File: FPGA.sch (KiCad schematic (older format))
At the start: 42 parts

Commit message: Reorganize FPGA schematic
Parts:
- added C?: 100n, symbol Device:C
- added J?: Conn_02x07_Odd_Even, symbol Connector_Generic:Conn_02x07_Odd_Even
- added R? (x2): 10k, symbol Device:R
- added R? (x4): 4.7k, symbol Device:R
- added R?: 330, symbol Device:R
- added R?: 2.4k, symbol Device:R
- added U? (x3): XC7A100T-FTG256, symbol FPGA_Xilinx_Artix7:XC7A100T-FTG256
- added U?: AS6C1616, Package_SO:TSOP-I-48_18.4x12mm_P0.5mm, symbol Memory_RAM:AS6C1616
- added U?: S25FL1, symbol flash_memory:S25FL1
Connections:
- net +3V3: now also C?.1, J?.2 (Pin_2), R?.1, R?.1, R?.1, R?.1, R?.1, R?.1, R?.1, R?.2, U?.37 (VCC), U?.8 (VCC), U?.A6 (VCCO_35), U?.B3 (VCCO_35), U?.D7 (VCCO_35), U?.E4 (VCCO_35), U?.E7 (CFGBVS_0), U?.F1 (VCCO_35), U?.J2 (VCCO_35), U?.L16 (VCCO_14), U?.L6 (VCCO_0), U?.M13 (VCCO_14), U?.M9 (M0_0), U?.N10 (VCCO_14), U?.P7 (VCCO_14), U?.R14 (VCCO_14), U?.T11 (VCCO_14)
- net GND: now also C?.2, J?.1 (Pin_1), J?.11 (Pin_11), J?.13 (Pin_13), J?.3 (Pin_3), J?.5 (Pin_5), J?.7 (Pin_7), J?.9 (Pin_9), U?.27 (VSS), U?.4 (GND), U?.46 (VSS), U?.A16 (VCCO_15), U?.B13 (VCCO_15), U?.C10 (VCCO_15), U?.E14 (VCCO_15), U?.H15 (VCCO_15), U?.H7 (VREFN_0), U?.H8 (VP_0), U?.J12 (VCCO_15), U?.J7 (VN_0), U?.J8 (VREFP_0), U?.M10 (M1_0), U?.M11 (M2_0), U?.M3 (VCCO_34), U?.R4 (VCCO_34), U?.T1 (VCCO_34)
- net at U?.5 (OUT): now also U?.N14 (IO_L12P_T1_MRCC_14)
- new net: U?.6 (CLK), U?.E8 (CCLK_0)
- new net: R?.2, U?.K10 (INIT_B_0)
- new net: J?.6 (Pin_6), R?.2, U?.L7 (TCK_0)
- new net: J?.4 (Pin_4), R?.2, U?.M7 (TMS_0)
- new net: J?.10 (Pin_10), U?.N7 (TDI_0)
- new net: J?.8 (Pin_8), U?.N8 (TDO_0)
- new net: U?.5 (SI/IO0), U?.J13 (IO_L1P_T0_D00_MOSI_14)
- new net: U?.2 (SO/IO1), U?.J14 (IO_L1N_T0_D01_DIN_14)
- new net: R?.2, U?.3 (WP#/IO2), U?.K15 (IO_L2P_T0_D02_14)
- new net: R?.2, U?.7 (HOLD#/RESET#/IO3), U?.K16 (IO_L2N_T0_D03_14)
- new net: R?.2, U?.1 (CS#), U?.L12 (IO_L6P_T0_FCS_B_14)
- new net SRAM_a0: U?.25 (A0), U?.A2 (IO_L8N_T1_AD14N_35)
- new net SRAM_a1: U?.24 (A1), U?.C1 (IO_L9P_T1_DQS_AD7P_35)
- new net SRAM_a10: U?.6 (A10), U?.E5 (IO_L13N_T2_MRCC_35)
- new net SRAM_a11: U?.5 (A11), U?.F4 (IO_L14P_T2_SRCC_35)
- new net SRAM_a12: U?.4 (A12), U?.F3 (IO_L14N_T2_SRCC_35)
- new net SRAM_a13: U?.3 (A13), U?.F2 (IO_L15P_T2_DQS_35)
- new net SRAM_a14: U?.2 (A14), U?.E1 (IO_L15N_T2_DQS_35)
- new net SRAM_a15: U?.1 (A15), U?.G5 (IO_L16P_T2_35)
- new net SRAM_a16: U?.48 (A16), U?.G4 (IO_L16N_T2_35)
- new net SRAM_a17: U?.17 (A17), U?.G2 (IO_L17P_T2_35)
- new net SRAM_a18: U?.16 (A18), U?.G1 (IO_L17N_T2_35)
- new net SRAM_a19: U?.9 (A19), U?.H5 (IO_L18P_T2_35)
- new net SRAM_a2: U?.23 (A2), U?.B1 (IO_L9N_T1_DQS_AD7N_35)
- new net SRAM_a3: U?.22 (A3), U?.E2 (IO_L10P_T1_AD15P_35)
- new net SRAM_a4: U?.21 (A4), U?.D1 (IO_L10N_T1_AD15N_35)
- new net SRAM_a5: U?.20 (A5), U?.E3 (IO_L11P_T1_SRCC_35)
- new net SRAM_a6: U?.19 (A6), U?.D3 (IO_L11N_T1_SRCC_35)
- new net SRAM_a7: U?.18 (A7), U?.D4 (IO_L12P_T1_MRCC_35)
- new net SRAM_a8: U?.8 (A8), U?.C4 (IO_L12N_T1_MRCC_35)
- new net SRAM_a9: U?.7 (A9), U?.F5 (IO_L13P_T2_MRCC_35)
- new net SRAM_ce#: U?.26 (CE#), U?.J4 (IO_L19N_T3_VREF_35)
- new net SRAM_ce2: U?.12 (CE2), U?.H2 (IO_L20P_T3_35)
- new net SRAM_dio0: U?.29 (DQ0), U?.E6 (IO_0_35)
- new net SRAM_dio1: U?.31 (DQ1), U?.B7 (IO_L1P_T0_AD4P_35)
- new net SRAM_dio10: U?.34 (DQ10), U?.C6 (IO_L5N_T0_AD13N_35)
- new net SRAM_dio11: U?.36 (DQ11), U?.D6 (IO_L6P_T0_35)
- new net SRAM_dio12: U?.39 (DQ12), U?.D5 (IO_L6N_T0_VREF_35)
- new net SRAM_dio13: U?.41 (DQ13), U?.C3 (IO_L7P_T1_AD6P_35)
- new net SRAM_dio14: U?.43 (DQ14), U?.C2 (IO_L7N_T1_AD6N_35)
- new net SRAM_dio15: U?.45 (DQ15), U?.B2 (IO_L8P_T1_AD14P_35)
- new net SRAM_dio2: U?.33 (DQ2), U?.A7 (IO_L1N_T0_AD4N_35)
- new net SRAM_dio3: U?.35 (DQ3), U?.B6 (IO_L2P_T0_AD12P_35)
- new net SRAM_dio4: U?.38 (DQ4), U?.B5 (IO_L2N_T0_AD12N_35)
- new net SRAM_dio5: U?.40 (DQ5), U?.A5 (IO_L3P_T0_DQS_AD5P_35)
- new net SRAM_dio6: U?.42 (DQ6), U?.A4 (IO_L3N_T0_DQS_AD5N_35)
- new net SRAM_dio7: U?.44 (DQ7), U?.B4 (IO_L4P_T0_35)
- new net SRAM_dio8: U?.30 (DQ8), U?.A3 (IO_L4N_T0_35)
- new net SRAM_dio9: U?.32 (DQ9), U?.C7 (IO_L5P_T0_AD13P_35)
- new net SRAM_lb#: U?.15 (LB#), U?.J3 (IO_L21P_T3_DQS_35)
- new net SRAM_oe#: U?.28 (OE#), U?.H4 (IO_L18N_T2_35)
- new net SRAM_ub#: U?.14 (UB#), U?.H1 (IO_L20N_T3_35)
- new net SRAM_we#: U?.11 (WE#), U?.J5 (IO_L19P_T3_35)
- new net done: R?.2, U?.H10 (DONE_0)
- new net program_b: R?.1, U?.L9 (PROGRAM_B_0)
- no-connect marks 1 -> 83
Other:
- moved on the sheet: C?, U?

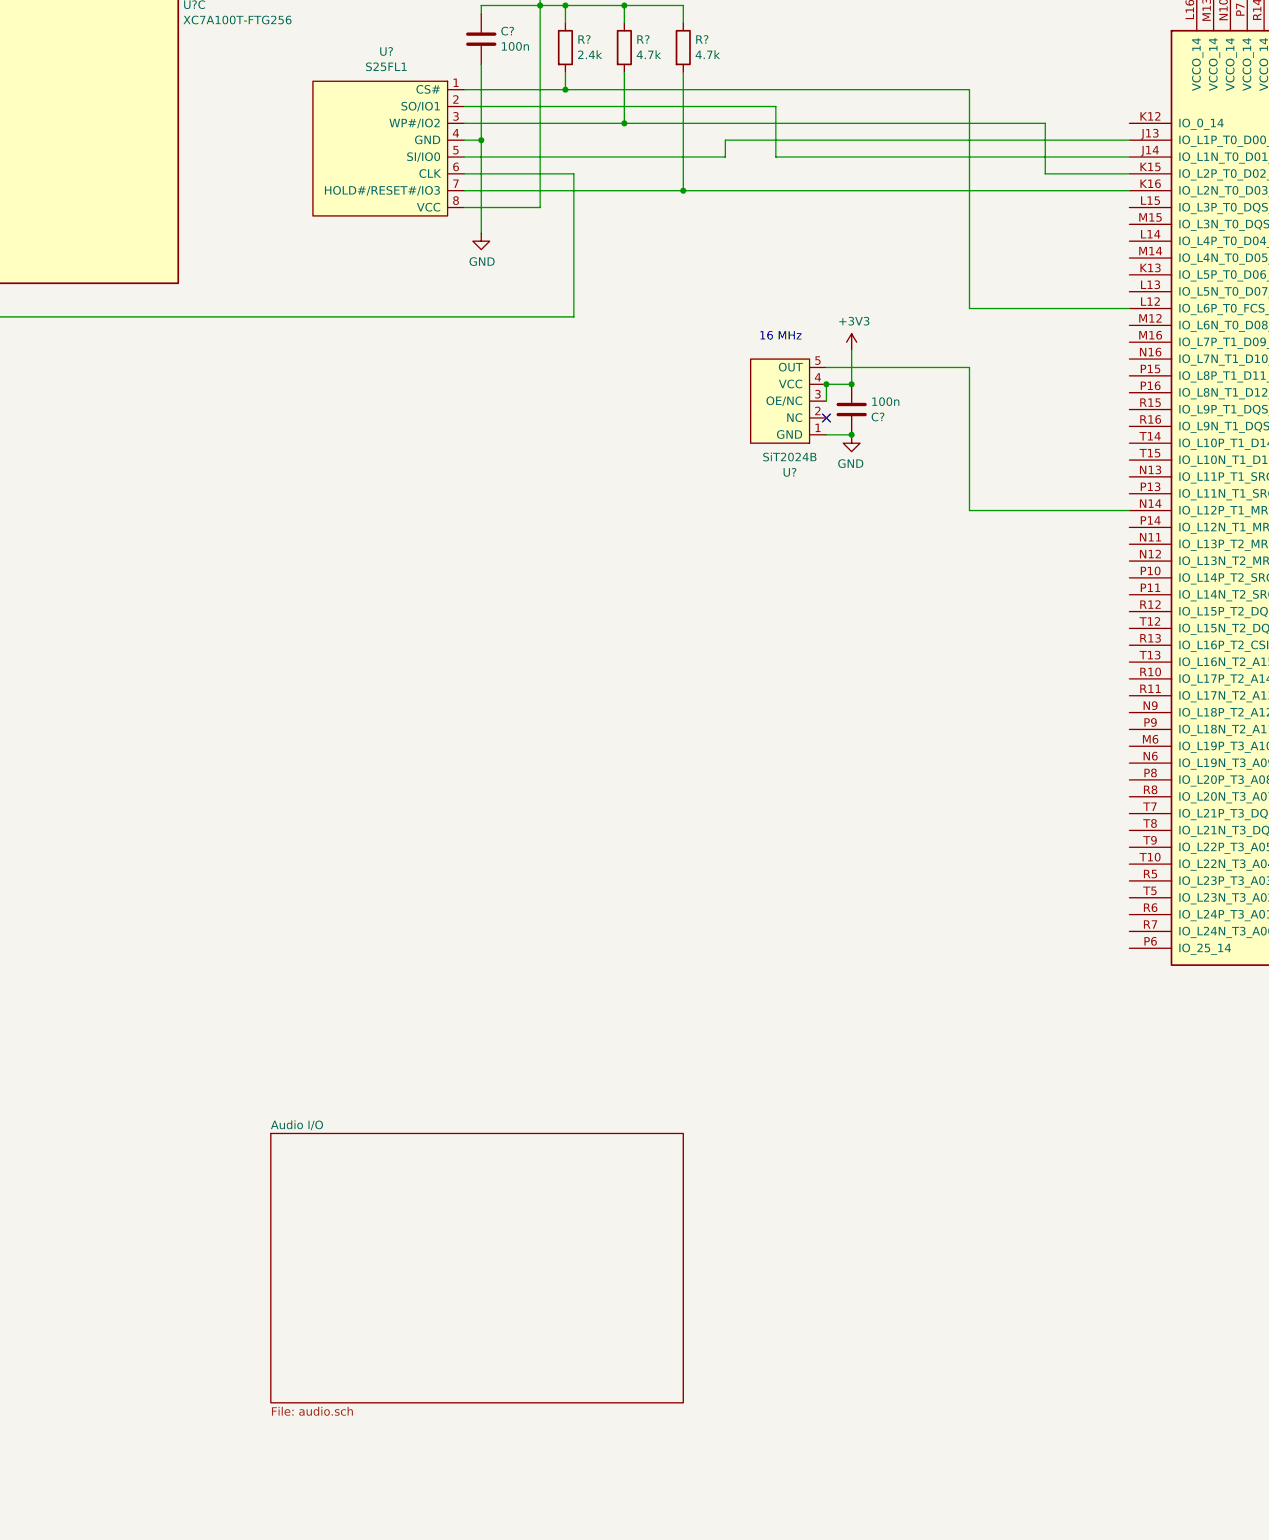
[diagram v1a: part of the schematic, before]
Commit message: Prepare FPGA I/O pins
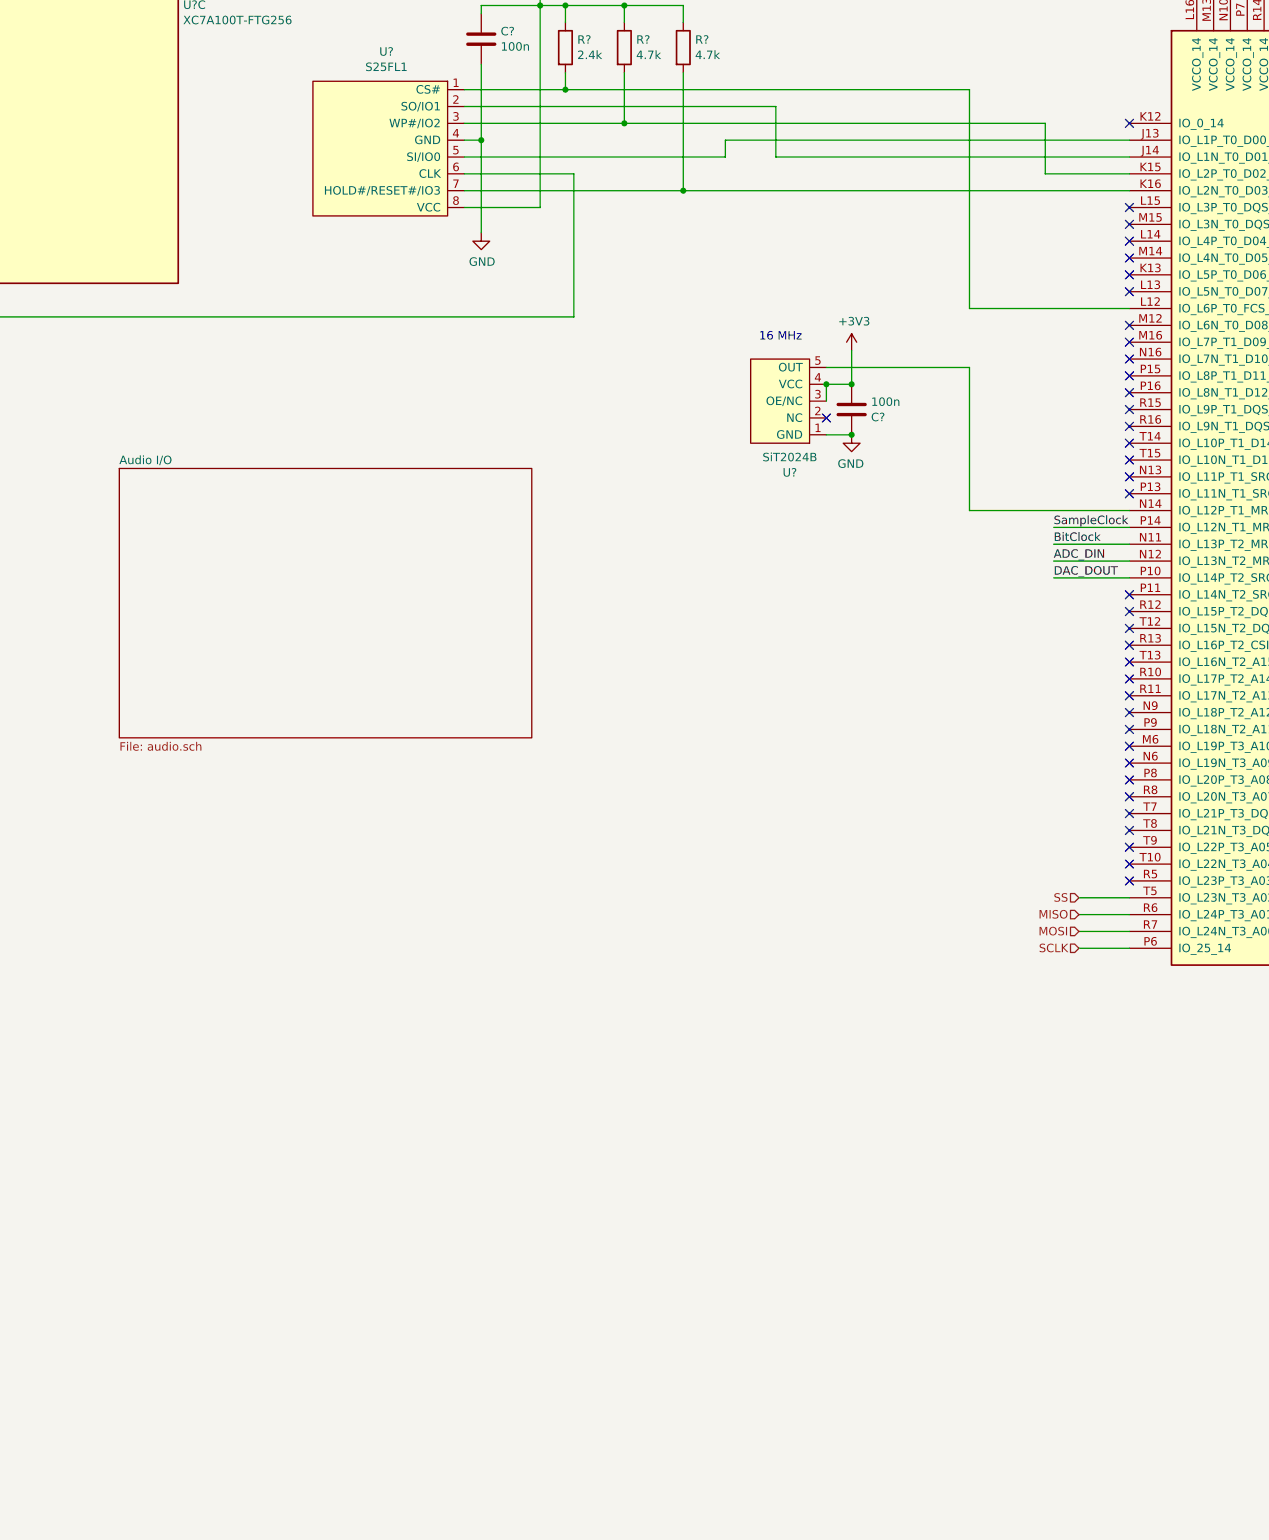
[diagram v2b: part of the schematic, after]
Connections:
- net BitClock: now reaches U?.N11 (IO_L13P_T2_MRCC_14)
- net ADC_DIN: now reaches U?.N12 (IO_L13N_T2_MRCC_14)
- net DAC_DOUT: now reaches U?.P10 (IO_L14P_T2_SRCC_14)
- net SampleClock: now reaches U?.P14 (IO_L12N_T1_MRCC_14)
- net SCLK: now reaches U?.P6 (IO_25_14)
- net MISO: now reaches U?.R6 (IO_L24P_T3_A01_D17_14)
- net MOSI: now reaches U?.R7 (IO_L24N_T3_A00_D16_14)
- net SS: now reaches U?.T5 (IO_L23N_T3_A02_D18_14)
- no-connect marks 83 -> 119
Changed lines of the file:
@@
 $EndDescr
 $Sheet
-S 1850 5950 2450 1600
+S 950  2000 2450 1600
 U 5D7E4A66
 F0 "Audio I/O" 50
@@
 Connection ~ 7600 13000
 $Comp
-L power:GND #PWR?
+L power:GND #PWR0124
 U 1 1 5E505D4A
 P 13450 1300
-AR Path="/5D7D43D9/5E505D4A" Ref="#PWR?"  Part="1"
+AR Path="/5D7D43D9/5E505D4A" Ref="#PWR0124"  Part="1"
 AR Path="/5D7D43D9/5DD5155F/5E505D4A" Ref="#PWR?"  Part="1"
 AR Path="/5D7D43D9/5E0EF1ED/5E505D4A" Ref="#PWR?"  Part="1"
-F 0 "#PWR?" H 13450 1050 50  0001 C CNN
+F 0 "#PWR0124" H 13450 1050 50  0001 C CNN
 F 1 "GND" H 13455 1127 50  0000 C CNN
 F 2 "" H 13450 1300 50  0001 C CNN
@@
 P 15550 1300
 AR Path="/5D7D43D9/5E0EF1ED/5E505D64" Ref="#PWR?"  Part="1"
-AR Path="/5D7D43D9/5E505D64" Ref="#PWR?"  Part="1"
-F 0 "#PWR?" H 15550 1150 50  0001 C CNN
+AR Path="/5D7D43D9/5E505D64" Ref="#PWR0125"  Part="1"
+F 0 "#PWR0125" H 15550 1150 50  0001 C CNN
 F 1 "+3V3" H 15565 1473 50  0000 C CNN
 F 2 "" H 15550 1300 50  0001 C CNN
@@
 P 19450 4450
 AR Path="/5D7D43D9/5E0EF1ED/5E505DDB" Ref="#PWR?"  Part="1"
-AR Path="/5D7D43D9/5E505DDB" Ref="#PWR?"  Part="1"
-F 0 "#PWR?" H 19450 4200 50  0001 C CNN
+AR Path="/5D7D43D9/5E505DDB" Ref="#PWR0126"  Part="1"
+F 0 "#PWR0126" H 19450 4200 50  0001 C CNN
 F 1 "GND" H 19455 4277 50  0000 C CNN
 F 2 "" H 19450 4450 50  0001 C CNN
@@
 P 19850 1400
 AR Path="/5D7D43D9/5E0EF1ED/5E505DED" Ref="#PWR?"  Part="1"
-AR Path="/5D7D43D9/5E505DED" Ref="#PWR?"  Part="1"
-F 0 "#PWR?" H 19850 1250 50  0001 C CNN
+AR Path="/5D7D43D9/5E505DED" Ref="#PWR0127"  Part="1"
+F 0 "#PWR0127" H 19850 1250 50  0001 C CNN
 F 1 "+3V3" H 19865 1573 50  0000 C CNN
 F 2 "" H 19850 1400 50  0001 C CNN
@@
 $EndComp
 $Comp
-L power:+3V3 #PWR?
+L power:+3V3 #PWR0128
 U 1 1 5E538FEB
 P -1050 -2450
-AR Path="/5D7D43D9/5E538FEB" Ref="#PWR?"  Part="1"
+AR Path="/5D7D43D9/5E538FEB" Ref="#PWR0128"  Part="1"
 AR Path="/5D7D43D9/5DD5155F/5E538FEB" Ref="#PWR?"  Part="1"
-F 0 "#PWR?" H -1050 -2600 50  0001 C CNN
+F 0 "#PWR0128" H -1050 -2600 50  0001 C CNN
 F 1 "+3V3" H -1035 -2277 50  0000 C CNN
 F 2 "" H -1050 -2450 50  0001 C CNN
@@
 P -4750 -250
 AR Path="/5D7D43D9/5DD5155F/5E538FF8" Ref="#PWR?"  Part="1"
-AR Path="/5D7D43D9/5E538FF8" Ref="#PWR?"  Part="1"
-F 0 "#PWR?" H -4750 -500 50  0001 C CNN
+AR Path="/5D7D43D9/5E538FF8" Ref="#PWR0129"  Part="1"
+F 0 "#PWR0129" H -4750 -500 50  0001 C CNN
 F 1 "GND" H -4745 -423 50  0000 C CNN
 F 2 "" H -4750 -250 50  0001 C CNN
@@
 P -3300 -2000
 AR Path="/5D7D43D9/5DD5155F/5E53900B" Ref="#PWR?"  Part="1"
-AR Path="/5D7D43D9/5E53900B" Ref="#PWR?"  Part="1"
-F 0 "#PWR?" H -3300 -2150 50  0001 C CNN
+AR Path="/5D7D43D9/5E53900B" Ref="#PWR0130"  Part="1"
+F 0 "#PWR0130" H -3300 -2150 50  0001 C CNN
 F 1 "+3V3" H -3285 -1827 50  0000 C CNN
 F 2 "" H -3300 -2000 50  0001 C CNN
@@
 P -1650 500
 AR Path="/5D7D43D9/5DD5155F/5E539066" Ref="#PWR?"  Part="1"
-AR Path="/5D7D43D9/5E539066" Ref="#PWR?"  Part="1"
-F 0 "#PWR?" H -1650 250 50  0001 C CNN
+AR Path="/5D7D43D9/5E539066" Ref="#PWR0131"  Part="1"
+F 0 "#PWR0131" H -1650 250 50  0001 C CNN
 F 1 "GND" H -1645 327 50  0000 C CNN
 F 2 "" H -1650 500 50  0001 C CNN
@@
 $EndComp
 $Comp
-L power:+3V3 #PWR?
+L power:+3V3 #PWR0132
 U 1 1 5E539084
 P 7350 -950
-AR Path="/5D7D43D9/5E539084" Ref="#PWR?"  Part="1"
+AR Path="/5D7D43D9/5E539084" Ref="#PWR0132"  Part="1"
 AR Path="/5D7D43D9/5DD5155F/5E539084" Ref="#PWR?"  Part="1"
-F 0 "#PWR?" H 7350 -1100 50  0001 C CNN
+F 0 "#PWR0132" H 7350 -1100 50  0001 C CNN
 F 1 "+3V3" H 7365 -777 50  0000 C CNN
 F 2 "" H 7350 -950 50  0001 C CNN
@@
 	10450 -850 10550 -850
 $Comp
-L power:GND #PWR?
+L power:GND #PWR0133
 U 1 1 5E53909E
 P 10750 -850
-AR Path="/5D7D43D9/5E53909E" Ref="#PWR?"  Part="1"
+AR Path="/5D7D43D9/5E53909E" Ref="#PWR0133"  Part="1"
 AR Path="/5D7D43D9/5DD5155F/5E53909E" Ref="#PWR?"  Part="1"
-F 0 "#PWR?" H 10750 -1100 50  0001 C CNN
+F 0 "#PWR0133" H 10750 -1100 50  0001 C CNN
 F 1 "GND" H 10755 -1023 50  0000 C CNN
 F 2 "" H 10750 -850 50  0001 C CNN
@@
 P 3450 -850
 AR Path="/5D7D43D9/5DD5155F/5E5390EE" Ref="#PWR?"  Part="1"
-AR Path="/5D7D43D9/5E5390EE" Ref="#PWR?"  Part="1"
-F 0 "#PWR?" H 3450 -1000 50  0001 C CNN
+AR Path="/5D7D43D9/5E5390EE" Ref="#PWR0134"  Part="1"
+F 0 "#PWR0134" H 3450 -1000 50  0001 C CNN
 F 1 "+3V3" H 3465 -677 50  0000 C CNN
 F 2 "" H 3450 -850 50  0001 C CNN
@@
 P 3100 600
 AR Path="/5D7D43D9/5DD5155F/5E53911A" Ref="#PWR?"  Part="1"
-AR Path="/5D7D43D9/5E53911A" Ref="#PWR?"  Part="1"
-F 0 "#PWR?" H 3100 350 50  0001 C CNN
+AR Path="/5D7D43D9/5E53911A" Ref="#PWR0135"  Part="1"
+F 0 "#PWR0135" H 3100 350 50  0001 C CNN
 F 1 "GND" H 3105 427 50  0000 C CNN
 F 2 "" H 3100 600 50  0001 C CNN
@@
 Wire Wire Line
 	6000 2250 6950 2250
+NoConn ~ 6950 -50
+NoConn ~ 6950 450
+NoConn ~ 6950 550
+NoConn ~ 6950 650
+NoConn ~ 6950 750
+NoConn ~ 6950 850
+NoConn ~ 6950 950
+Text Label 6500 2350 0    50   ~ 0
+SampleClock
+Wire Wire Line
+	6950 2350 6500 2350
+Text Label 6500 2450 0    50   ~ 0
+BitClock
+Wire Wire Line
+	6500 2450 6950 2450
+Text Label 6500 2550 0    50   ~ 0
+ADC_DIN
+Wire Wire Line
+	6500 2550 6950 2550
+Text Label 6500 2650 0    50   ~ 0
+DAC_DOUT
+Wire Wire Line
+	6500 2650 6950 2650
+Text HLabel 6650 4850 0    50   Input ~ 0
+SCLK
+Text HLabel 6650 4750 0    50   Input ~ 0
+MOSI
+Text HLabel 6650 4650 0    50   Input ~ 0
+MISO
+Text HLabel 6650 4550 0    50   Input ~ 0
+SS
+Wire Wire Line
+	6650 4550 6950 4550
+Wire Wire Line
+	6650 4650 6950 4650
+Wire Wire Line
+	6650 4750 6950 4750
+Wire Wire Line
+	6650 4850 6950 4850
+NoConn ~ 6950 1150
+NoConn ~ 6950 1250
+NoConn ~ 6950 1350
+NoConn ~ 6950 1450
+NoConn ~ 6950 1550
+NoConn ~ 6950 1650
+NoConn ~ 6950 1750
+NoConn ~ 6950 1850
+NoConn ~ 6950 1950
+NoConn ~ 6950 2050
+NoConn ~ 6950 2150
+NoConn ~ 6950 2750
+NoConn ~ 6950 2850
+NoConn ~ 6950 2950
+NoConn ~ 6950 3050
+NoConn ~ 6950 3150
+NoConn ~ 6950 3250
+NoConn ~ 6950 3350
+NoConn ~ 6950 3450
+NoConn ~ 6950 3550
+NoConn ~ 6950 3650
+NoConn ~ 6950 3750
+NoConn ~ 6950 3850
+NoConn ~ 6950 3950
+NoConn ~ 6950 4050
+NoConn ~ 6950 4150
+NoConn ~ 6950 4250
+NoConn ~ 6950 4350
+NoConn ~ 6950 4450
 $EndSCHEMATC

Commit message: FPGA cleanup
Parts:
- added J2: 26642801RP2, CON28_2X14_HDR_2664, symbol pin_header:26642801RP2
- U3: renamed from U?; footprint (none) -> Package_BGA:Xilinx_FTG256
- U4: renamed from U?; footprint (none) -> Package_SO:SOIC-8_5.275x5.275mm_P1.27mm
- U5: renamed from U?; footprint (none) -> Package_TO_SOT_SMD:SOT-23-5
- gave numbers to parts that had none: 52
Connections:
- net ADC_DIN: now also U3.M14 (IO_L4N_T0_D05_14); no longer U3.N12 (IO_L13N_T2_MRCC_14)
- net BitClock: now also U3.L14 (IO_L4P_T0_D04_14); no longer U3.N11 (IO_L13P_T2_MRCC_14)
- net DAC_DOUT: now also U3.K13 (IO_L5P_T0_D06_14); no longer U3.P10 (IO_L14P_T2_SRCC_14)
- net MISO: now also U3.R15 (IO_L9P_T1_DQS_14); no longer U3.R6 (IO_L24P_T3_A01_D17_14)
- net MOSI: now also U3.R16 (IO_L9N_T1_DQS_D13_14); no longer U3.R7 (IO_L24N_T3_A00_D16_14)
- net SCLK: now also U3.T14 (IO_L10P_T1_D14_14); no longer U3.P6 (IO_25_14)
- net SS: now also U3.P16 (IO_L8N_T1_D12_14); no longer U3.T5 (IO_L23N_T3_A02_D18_14)
- net SampleClock: now also U3.M15 (IO_L3N_T0_DQS_EMCCLK_14); no longer U3.P14 (IO_L12N_T1_MRCC_14)
- net GPIO_3: now reaches U3.M12 (IO_L6N_T0_D08_VREF_14)
- net GPIO_2: now reaches U3.M16 (IO_L7P_T1_D09_14)
- net FPGA_pinout_14: now reaches U3.M6 (IO_L19P_T3_A10_D26_14)
- net FPGA_pinout_14: now also J2.14
- net GPIO_1: now reaches U3.N16 (IO_L7N_T1_D10_14)
- net FPGA_pinout_15: now reaches U3.N6 (IO_L19N_T3_A09_D25_VREF_14)
- net FPGA_pinout_15: now also J2.15
- net FPGA_pinout_12: now reaches U3.N9 (IO_L18P_T2_A12_D28_14)
- net FPGA_pinout_12: now also J2.12
- net FPGA_pinout_5: now reaches U3.P11 (IO_L14N_T2_SRCC_14)
- net FPGA_pinout_5: now also J2.5
- net GPIO_0: now reaches U3.P15 (IO_L8P_T1_D11_14)
- net FPGA_pinout_16: now reaches U3.P8 (IO_L20P_T3_A08_D24_14)
- net FPGA_pinout_16: now also J2.16
- net FPGA_pinout_13: now reaches U3.P9 (IO_L18N_T2_A11_D27_14)
- net FPGA_pinout_13: now also J2.13
- net FPGA_pinout_10: now reaches U3.R10 (IO_L17P_T2_A14_D30_14)
- net FPGA_pinout_10: now also J2.10
- net FPGA_pinout_11: now reaches U3.R11 (IO_L17N_T2_A13_D29_14)
- net FPGA_pinout_11: now also J2.11
- net FPGA_pinout_6: now reaches U3.R12 (IO_L15P_T2_DQS_RDWR_B_14)
- net FPGA_pinout_6: now also J2.6
- net FPGA_pinout_8: now reaches U3.R13 (IO_L16P_T2_CSI_B_14)
- net FPGA_pinout_8: now also J2.8
- net FPGA_pinout_22: now reaches U3.R5 (IO_L23P_T3_A03_D19_14)
- net FPGA_pinout_22: now also J2.22
- net FPGA_pinout_17: now reaches U3.R8 (IO_L20N_T3_A07_D23_14)
- net FPGA_pinout_17: now also J2.17
- net FPGA_pinout_21: now reaches U3.T10 (IO_L22N_T3_A04_D20_14)
- net FPGA_pinout_21: now also J2.21
- net FPGA_pinout_7: now reaches U3.T12 (IO_L15N_T2_DQS_DOUT_CSO_B_14)
- net FPGA_pinout_7: now also J2.7
- net FPGA_pinout_9: now reaches U3.T13 (IO_L16N_T2_A15_D31_14)
- net FPGA_pinout_9: now also J2.9
- net FPGA_pinout_18: now reaches U3.T7 (IO_L21P_T3_DQS_14)
- net FPGA_pinout_18: now also J2.18
- net FPGA_pinout_19: now reaches U3.T8 (IO_L21N_T3_DQS_A06_D22_14)
- net FPGA_pinout_19: now also J2.19
- net FPGA_pinout_20: now reaches U3.T9 (IO_L22P_T3_A05_D21_14)
- net FPGA_pinout_20: now also J2.20
- new net FPGA_pinout_1: J2.1, U3.P14 (IO_L12N_T1_MRCC_14)
- new net FPGA_pinout_2: J2.2, U3.N11 (IO_L13P_T2_MRCC_14)
- new net FPGA_pinout_23: J2.23, U3.T5 (IO_L23N_T3_A02_D18_14)
- new net FPGA_pinout_24: J2.24, U3.R6 (IO_L24P_T3_A01_D17_14)
- new net FPGA_pinout_25: J2.25, U3.R7 (IO_L24N_T3_A00_D16_14)
- new net FPGA_pinout_26: J2.26, U3.P6 (IO_25_14)
- new net FPGA_pinout_3: J2.3, U3.N12 (IO_L13N_T2_MRCC_14)
- new net FPGA_pinout_4: J2.4, U3.P10 (IO_L14P_T2_SRCC_14)
- no-connect marks 119 -> 91
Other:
- note added: "Vccaux"
- note added: "Vccbram"
- note added: "Vcco"
- moved on the sheet: C20, C25, J1, R10, R11, R12, R13, R14, R15, R16, R17, U3A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
